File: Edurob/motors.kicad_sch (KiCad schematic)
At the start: 24 parts, among them IC1 TC78H660FTG,EL, IC2 TC78H660FTG,EL

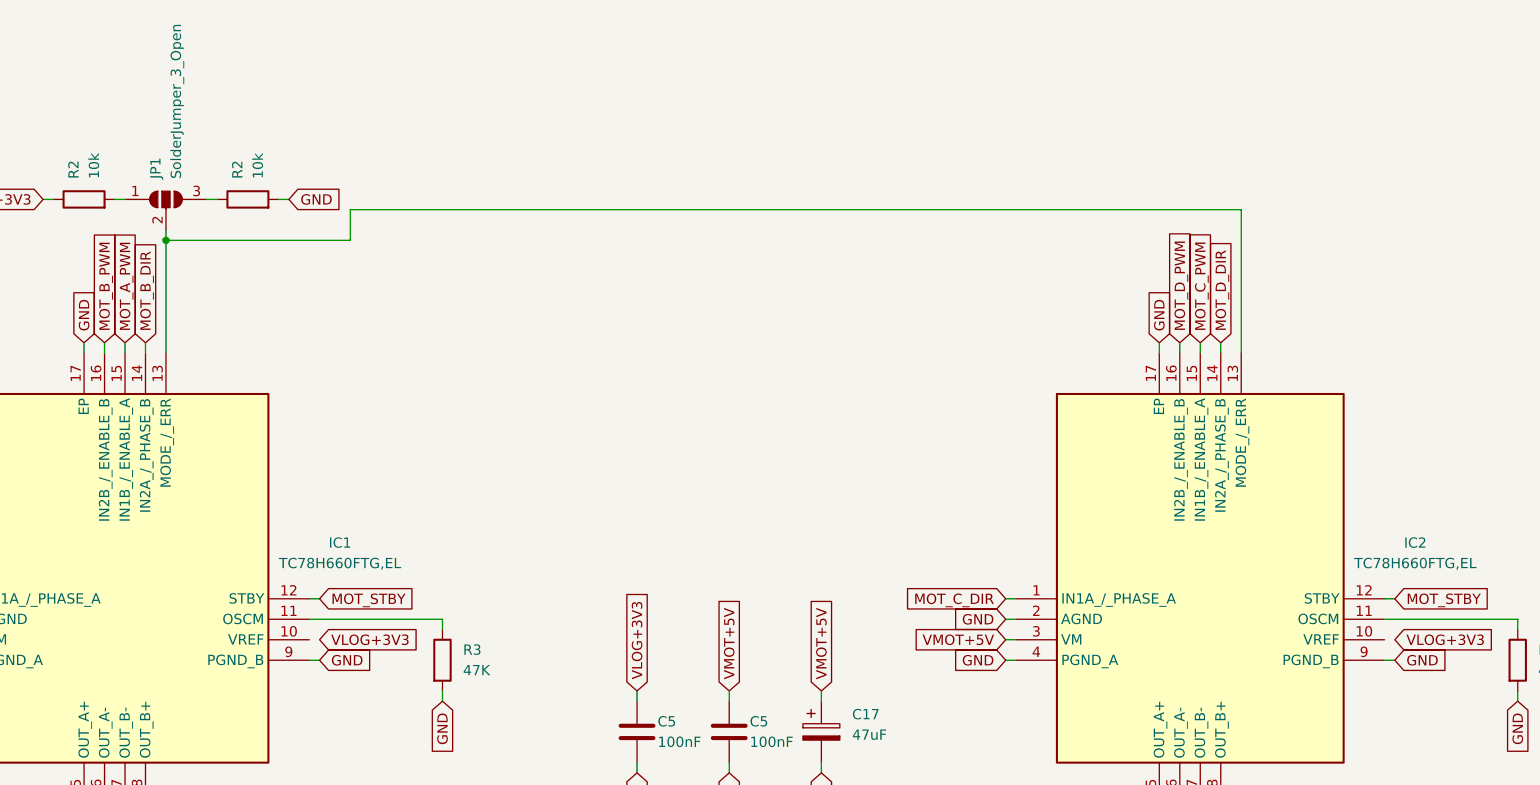
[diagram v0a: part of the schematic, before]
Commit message: Added GPIO Expander, finalized Connector positions
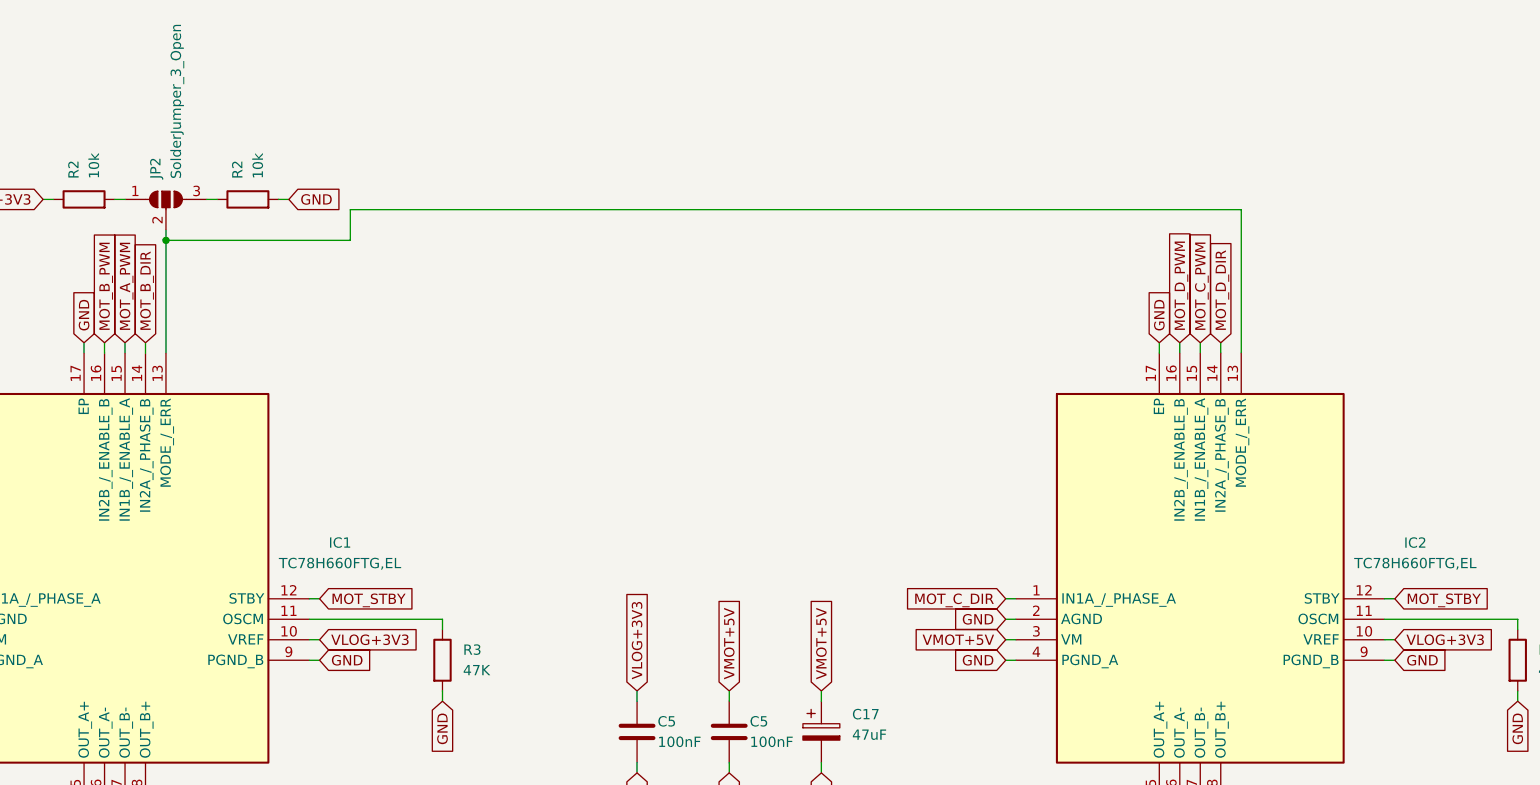
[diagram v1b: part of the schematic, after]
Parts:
- renumbered JP1 to JP2
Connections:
- net VLOG+3V3: now also IC1.10 (VREF), IC2.10 (VREF)
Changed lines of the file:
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@@
+    (stroke (width 0) (type default))
+  )
+  (wire (pts (xy 124.46 104.14) (xy 125.73 104.14))
     (stroke (width 0) (type default))
   )
@@
   )
   (wire (pts (xy 52.07 161.29) (xy 52.07 163.83))
+    (stroke (width 0) (type default))
+  )
+  (wire (pts (xy 257.81 104.14) (xy 259.08 104.14))
     (stroke (width 0) (type default))
   )
@@
       )
       (project "Edurob"
-        (path "/ea495553-3cd2-4380-af57-b7ab16ec3dc9/89de68d6-46a2-4637-9552-cf7ed3825f2a"
-          (reference "R7") (unit 1)
-        )
         (path "/ea495553-3cd2-4380-af57-b7ab16ec3dc9/b565ef5e-ebd0-4632-9832-ca713cd7c533"
           (reference "R19") (unit 1)
@@
       )
       (project "Edurob"
-        (path "/ea495553-3cd2-4380-af57-b7ab16ec3dc9"
-          (reference "R1") (unit 1)
-        )
-        (path "/ea495553-3cd2-4380-af57-b7ab16ec3dc9/8aa2f8b0-d8d3-42d6-a936-678d5127e1c2"
-          (reference "R4") (unit 1)
-        )
-        (path "/ea495553-3cd2-4380-af57-b7ab16ec3dc9/172d60ec-c5c3-4534-881f-0378b6cc8d8f"
-          (reference "R5") (unit 1)
-        )
         (path "/ea495553-3cd2-4380-af57-b7ab16ec3dc9/b565ef5e-ebd0-4632-9832-ca713cd7c533"
           (reference "R15") (unit 1)
@@
       )
       (project "Edurob"
-        (path "/ea495553-3cd2-4380-af57-b7ab16ec3dc9"
-          (reference "R1") (unit 1)
-        )
-        (path "/ea495553-3cd2-4380-af57-b7ab16ec3dc9/8aa2f8b0-d8d3-42d6-a936-678d5127e1c2"
-          (reference "R4") (unit 1)
-        )
-        (path "/ea495553-3cd2-4380-af57-b7ab16ec3dc9/172d60ec-c5c3-4534-881f-0378b6cc8d8f"
-          (reference "R6") (unit 1)
-        )
         (path "/ea495553-3cd2-4380-af57-b7ab16ec3dc9/b565ef5e-ebd0-4632-9832-ca713cd7c533"
           (reference "R21") (unit 1)
@@
       )
       (project "Edurob"
-        (path "/ea495553-3cd2-4380-af57-b7ab16ec3dc9"
-          (reference "R1") (unit 1)
-        )
-        (path "/ea495553-3cd2-4380-af57-b7ab16ec3dc9/8aa2f8b0-d8d3-42d6-a936-678d5127e1c2"
-          (reference "R4") (unit 1)
-        )
-        (path "/ea495553-3cd2-4380-af57-b7ab16ec3dc9/172d60ec-c5c3-4534-881f-0378b6cc8d8f"
-          (reference "R6") (unit 1)
-        )
         (path "/ea495553-3cd2-4380-af57-b7ab16ec3dc9/b565ef5e-ebd0-4632-9832-ca713cd7c533"
           (reference "R14") (unit 1)
@@
       )
       (project "Edurob"
-        (path "/ea495553-3cd2-4380-af57-b7ab16ec3dc9/3d6529d3-09ba-43bd-8600-e24f0f302957"
-          (reference "C3") (unit 1)
-        )
         (path "/ea495553-3cd2-4380-af57-b7ab16ec3dc9/b565ef5e-ebd0-4632-9832-ca713cd7c533"
           (reference "C14") (unit 1)
@@
       )
       (project "Edurob"
-        (path "/ea495553-3cd2-4380-af57-b7ab16ec3dc9/89de68d6-46a2-4637-9552-cf7ed3825f2a"
-          (reference "R7") (unit 1)
-        )
         (path "/ea495553-3cd2-4380-af57-b7ab16ec3dc9/b565ef5e-ebd0-4632-9832-ca713cd7c533"
           (reference "R12") (unit 1)
@@
       )
       (project "Edurob"
-        (path "/ea495553-3cd2-4380-af57-b7ab16ec3dc9/3d6529d3-09ba-43bd-8600-e24f0f302957"
-          (reference "C3") (unit 1)
-        )
         (path "/ea495553-3cd2-4380-af57-b7ab16ec3dc9/b565ef5e-ebd0-4632-9832-ca713cd7c533"
           (reference "C16") (unit 1)
@@
       )
       (project "Edurob"
-        (path "/ea495553-3cd2-4380-af57-b7ab16ec3dc9"
-          (reference "R1") (unit 1)
-        )
-        (path "/ea495553-3cd2-4380-af57-b7ab16ec3dc9/8aa2f8b0-d8d3-42d6-a936-678d5127e1c2"
-          (reference "R4") (unit 1)
-        )
-        (path "/ea495553-3cd2-4380-af57-b7ab16ec3dc9/172d60ec-c5c3-4534-881f-0378b6cc8d8f"
-          (reference "R6") (unit 1)
-        )
         (path "/ea495553-3cd2-4380-af57-b7ab16ec3dc9/b565ef5e-ebd0-4632-9832-ca713cd7c533"
           (reference "R23") (unit 1)
@@
       )
       (project "Edurob"
-        (path "/ea495553-3cd2-4380-af57-b7ab16ec3dc9"
-          (reference "R1") (unit 1)
-        )
-        (path "/ea495553-3cd2-4380-af57-b7ab16ec3dc9/8aa2f8b0-d8d3-42d6-a936-678d5127e1c2"
-          (reference "R4") (unit 1)
-        )
-        (path "/ea495553-3cd2-4380-af57-b7ab16ec3dc9/172d60ec-c5c3-4534-881f-0378b6cc8d8f"
-          (reference "R6") (unit 1)
-        )
         (path "/ea495553-3cd2-4380-af57-b7ab16ec3dc9/b565ef5e-ebd0-4632-9832-ca713cd7c533"
           (reference "R25") (unit 1)
@@
       )
       (project "Edurob"
-        (path "/ea495553-3cd2-4380-af57-b7ab16ec3dc9/89de68d6-46a2-4637-9552-cf7ed3825f2a"
-          (reference "R7") (unit 1)
-        )
         (path "/ea495553-3cd2-4380-af57-b7ab16ec3dc9/b565ef5e-ebd0-4632-9832-ca713cd7c533"
           (reference "R13") (unit 1)
@@
       )
       (project "Edurob"
-        (path "/ea495553-3cd2-4380-af57-b7ab16ec3dc9"
-          (reference "R1") (unit 1)
-        )
-        (path "/ea495553-3cd2-4380-af57-b7ab16ec3dc9/8aa2f8b0-d8d3-42d6-a936-678d5127e1c2"
-          (reference "R4") (unit 1)
-        )
-        (path "/ea495553-3cd2-4380-af57-b7ab16ec3dc9/172d60ec-c5c3-4534-881f-0378b6cc8d8f"
-          (reference "R6") (unit 1)
-        )
         (path "/ea495553-3cd2-4380-af57-b7ab16ec3dc9/b565ef5e-ebd0-4632-9832-ca713cd7c533"
           (reference "R16") (unit 1)
@@
       )
       (project "Edurob"
-        (path "/ea495553-3cd2-4380-af57-b7ab16ec3dc9"
-          (reference "R1") (unit 1)
-        )
-        (path "/ea495553-3cd2-4380-af57-b7ab16ec3dc9/8aa2f8b0-d8d3-42d6-a936-678d5127e1c2"
-          (reference "R4") (unit 1)
-        )
-        (path "/ea495553-3cd2-4380-af57-b7ab16ec3dc9/172d60ec-c5c3-4534-881f-0378b6cc8d8f"
-          (reference "R6") (unit 1)
-        )
         (path "/ea495553-3cd2-4380-af57-b7ab16ec3dc9/b565ef5e-ebd0-4632-9832-ca713cd7c533"
           (reference "R18") (unit 1)
@@
   (symbol (lib_id "Jumper:SolderJumper_3_Open") (at 106.68 49.53 0) (unit 1)
     (in_bom yes) (on_board yes) (dnp no) (fields_autoplaced)
-    (property "Reference" "JP1" (at 105.41 46.99 90)
+    (property "Reference" "JP2" (at 105.41 46.99 90)
       (effects (font (size 1.27 1.27)) (justify left))
     )
@@
     (instances
       (project "Edurob"
-        (path "/ea495553-3cd2-4380-af57-b7ab16ec3dc9/172d60ec-c5c3-4534-881f-0378b6cc8d8f"
-          (reference "JP1") (unit 1)
-        )
         (path "/ea495553-3cd2-4380-af57-b7ab16ec3dc9/b565ef5e-ebd0-4632-9832-ca713cd7c533"
           (reference "JP2") (unit 1)
@@
       )
       (project "Edurob"
-        (path "/ea495553-3cd2-4380-af57-b7ab16ec3dc9/3d6529d3-09ba-43bd-8600-e24f0f302957"
-          (reference "C3") (unit 1)
-        )
         (path "/ea495553-3cd2-4380-af57-b7ab16ec3dc9/b565ef5e-ebd0-4632-9832-ca713cd7c533"
           (reference "C13") (unit 1)
@@
       )
       (project "Edurob"
-        (path "/ea495553-3cd2-4380-af57-b7ab16ec3dc9/3d6529d3-09ba-43bd-8600-e24f0f302957"
-          (reference "C3") (unit 1)
-        )
         (path "/ea495553-3cd2-4380-af57-b7ab16ec3dc9/b565ef5e-ebd0-4632-9832-ca713cd7c533"
           (reference "C15") (unit 1)
@@
       )
       (project "Edurob"
-        (path "/ea495553-3cd2-4380-af57-b7ab16ec3dc9"
-          (reference "R1") (unit 1)
-        )
-        (path "/ea495553-3cd2-4380-af57-b7ab16ec3dc9/8aa2f8b0-d8d3-42d6-a936-678d5127e1c2"
-          (reference "R4") (unit 1)
-        )
-        (path "/ea495553-3cd2-4380-af57-b7ab16ec3dc9/172d60ec-c5c3-4534-881f-0378b6cc8d8f"
-          (reference "R6") (unit 1)
-        )
         (path "/ea495553-3cd2-4380-af57-b7ab16ec3dc9/b565ef5e-ebd0-4632-9832-ca713cd7c533"
           (reference "R24") (unit 1)
@@
       )
       (project "Edurob"
-        (path "/ea495553-3cd2-4380-af57-b7ab16ec3dc9"
-          (reference "R1") (unit 1)
-        )
-        (path "/ea495553-3cd2-4380-af57-b7ab16ec3dc9/8aa2f8b0-d8d3-42d6-a936-678d5127e1c2"
-          (reference "R4") (unit 1)
-        )
-        (path "/ea495553-3cd2-4380-af57-b7ab16ec3dc9/172d60ec-c5c3-4534-881f-0378b6cc8d8f"
-          (reference "R6") (unit 1)
-        )
         (path "/ea495553-3cd2-4380-af57-b7ab16ec3dc9/b565ef5e-ebd0-4632-9832-ca713cd7c533"
           (reference "R17") (unit 1)
@@
       )
       (project "Edurob"
-        (path "/ea495553-3cd2-4380-af57-b7ab16ec3dc9"
-          (reference "R1") (unit 1)
-        )
-        (path "/ea495553-3cd2-4380-af57-b7ab16ec3dc9/8aa2f8b0-d8d3-42d6-a936-678d5127e1c2"
-          (reference "R4") (unit 1)
-        )
-        (path "/ea495553-3cd2-4380-af57-b7ab16ec3dc9/172d60ec-c5c3-4534-881f-0378b6cc8d8f"
-          (reference "R6") (unit 1)
-        )
         (path "/ea495553-3cd2-4380-af57-b7ab16ec3dc9/b565ef5e-ebd0-4632-9832-ca713cd7c533"
           (reference "R20") (unit 1)
@@
       )
       (project "Edurob"
-        (path "/ea495553-3cd2-4380-af57-b7ab16ec3dc9"
-          (reference "R1") (unit 1)
-        )
-        (path "/ea495553-3cd2-4380-af57-b7ab16ec3dc9/8aa2f8b0-d8d3-42d6-a936-678d5127e1c2"
-          (reference "R4") (unit 1)
-        )
-        (path "/ea495553-3cd2-4380-af57-b7ab16ec3dc9/172d60ec-c5c3-4534-881f-0378b6cc8d8f"
-          (reference "R6") (unit 1)
-        )
         (path "/ea495553-3cd2-4380-af57-b7ab16ec3dc9/b565ef5e-ebd0-4632-9832-ca713cd7c533"
           (reference "R22") (unit 1)

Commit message: Release v1.0.1
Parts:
- C12, C17: Manufacturer_Name (none) -> KEMET; Manufacturer_Part_Number (none) -> T491X476K035AT; Mouser Part Number (none) -> 80-T491X476K035; Mouser Price/Stock (none) -> https://www.mouser.de/ProductDetail/80-T491X476K035; Placed (none) -> True
- C5: Manufacturer_Name (none) -> KYOCERA AVX; Manufacturer_Part_Number (none) -> KGM15BR71E104KT; Mouser Part Number (none) -> 581-KGM15BR71E104KT; Mouser Price/Stock (none) -> https://www.mouser.de/ProductDetail/581-KGM15BR71E104KT; Placed (none) -> True
- D2: Manufacturer_Name (none) -> ams OSRAM; Manufacturer_Part_Number (none) -> LO Q976.01-P2R2-25-1; Mouser Part Number (none) -> 720-LOQ976.01P2R2251; Mouser Price/Stock (none) -> https://www.mouser.de/ProductDetail/720-LOQ976.01P2R2251; Placed (none) -> True
- IC1, IC2: Arrow Part Number TC78H660FTG,EL -> (none); Arrow Price/Stock https://www.arrow.com/en/products/tc78h660ftgel/toshiba?reg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 -> (none); Height 0.9 -> (none); Manufacturer_Part_Number TC78H660FTG,EL -> TC78H660FTGEL; Mouser Price/Stock https://www.mouser.co.uk/ProductDetail/Toshiba/TC78H660FTGE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 -> https://www.mouser.de/ProductDetail/757-TC78H660FTGEL; Placed (none) -> True
- JP2: Placed (none) -> False
- R2: value 10k -> 10K; Manufacturer_Name (none) -> Vishay / Dale; Manufacturer_Part_Number (none) -> CRCW060310K0FKEA; Mouser Part Number (none) -> 71-CRCW0603-10K-E3; Mouser Price/Stock (none) -> https://www.mouser.de/ProductDetail/71-CRCW0603-10K-E3; Placed (none) -> True
- R2: Manufacturer_Name (none) -> Vishay / Dale; Manufacturer_Part_Number (none) -> CRCW0603130RFKEA; Mouser Part Number (none) -> 71-CRCW0603-130-E3; Mouser Price/Stock (none) -> https://www.mouser.de/ProductDetail/71-CRCW0603-130-E3; Placed (none) -> True
- R3: Manufacturer_Name (none) -> Vishay / Dale; Manufacturer_Part_Number (none) -> CRCW060347K0FKEA; Mouser Part Number (none) -> 71-CRCW0603-47K-E3; Mouser Price/Stock (none) -> https://www.mouser.de/ProductDetail/71-CRCW0603-47K-E3; Placed (none) -> True
- R3: Manufacturer_Name (none) -> Vishay / Dale; Manufacturer_Part_Number (none) -> CRCW060310K0FKEA; Mouser Part Number (none) -> 71-CRCW0603-10K-E3; Mouser Price/Stock (none) -> https://www.mouser.de/ProductDetail/71-CRCW0603-10K-E3; Placed (none) -> True
